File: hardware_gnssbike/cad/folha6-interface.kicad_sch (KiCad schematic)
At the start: 22 parts, among them Q601 DMG1012T-7, Q602 DMG1012T-7, Q603 DMG1012T-7, SW601 XunPu TS-1088R-02026, SW602 XunPu TS-1088R-02026, SW603 XunPu TS-1088R-02026

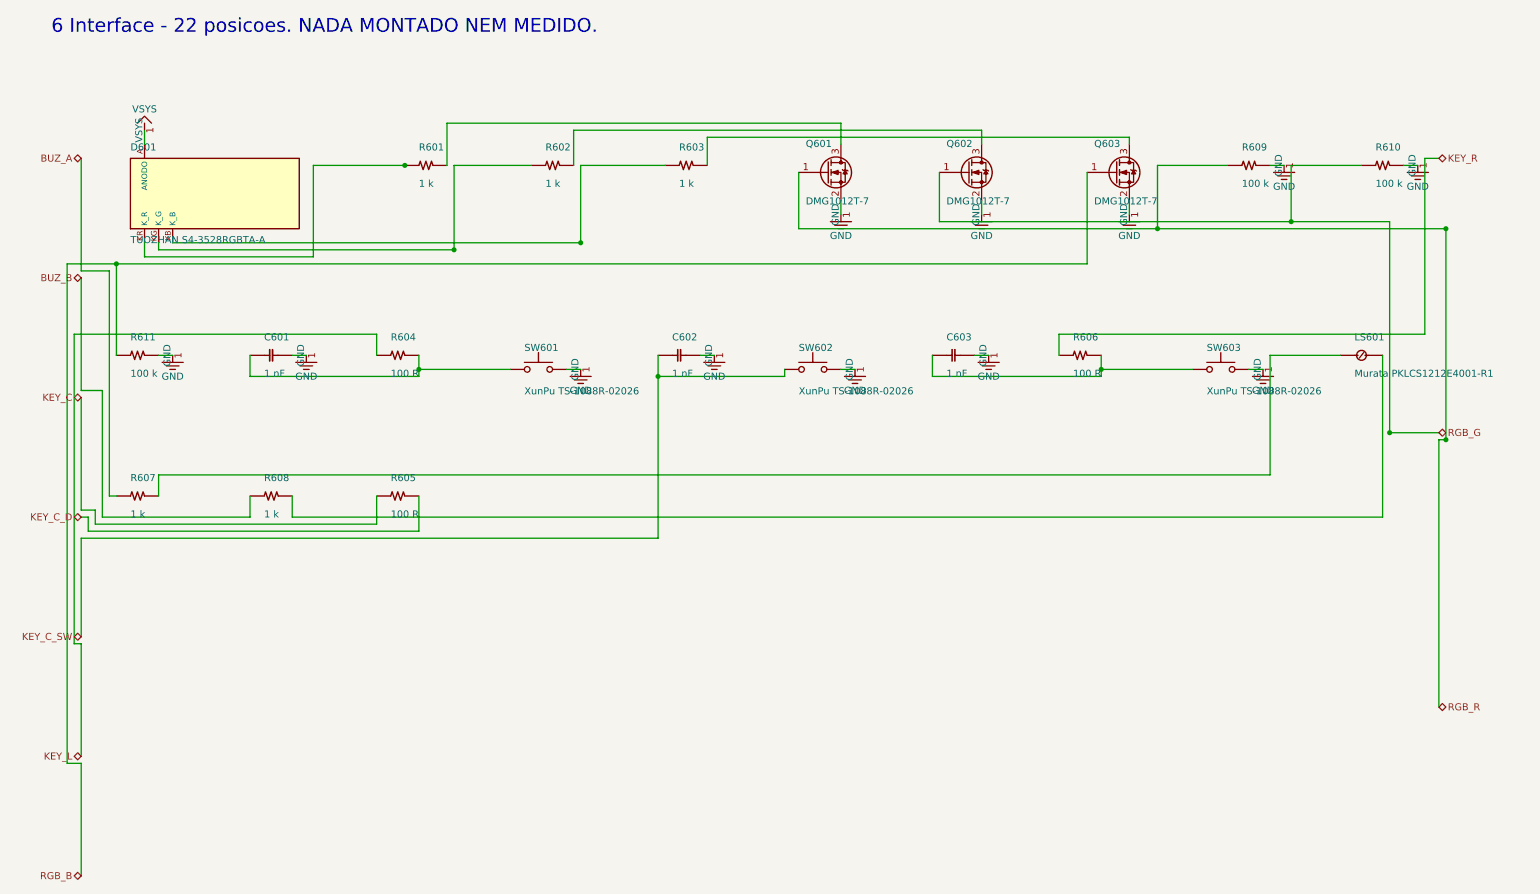
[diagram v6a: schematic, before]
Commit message: feat(hardware): draw the schematic by functional block, the way a person reads it
The owner asked for an industrial-standard schematic: wires and labels,
A4 or A3 pages, the right symbols and values, easy to read, the circuits
subdivided by dashed boxes. Until now each sheet was the netlist drawn as
wires - parts on a grid in connection order and a maze router pulling a
wire from every pin to wherever its other end was, across the page.

blocos.py turns each sheet into a row of functional blocks in the order
the signal flows, each in a dashed rectangle with a title: on the power
sheet, USB-C and protection, the nPM1300, the gauge and the cell, the GNSS
backup, the solar harvester, the thermal cut-off. Membership comes from
the BLOCOS table (the anchors), then make_pcb.DECOPLA and JUNTO (the
board already says whose each capacitor is), then sheets.SEGUE, then the
netlist without rails, nearest anchor by hops. Inside a block the anchor
sits in the middle and each passive beside the pin it serves, on the
side that pin faces, mirrored when the pin that serves the chip is the
far one; parts that touch only rails go to a shelf under the chip. Rails
are power symbols, neighbouring pins of one rail get a wire along their
tips and one symbol; a net that leaves its block is a local label, one
that leaves the sheet a hierarchical label, both on a short stub the
maze router bends when the straight way is taken. Sheet 1 is A3, the
rest A4, measured by the drawing itself. Decoupling capacitors now live
on their chip's sheet whatever their number.

Three KiCad 8 facts were measured with kicad-cli's netlist export on the
way, because the first version assumed each one wrong and check_sch.py
caught it: (mirror x) swaps left for right, not (mirror y); a local label
named after a rail is the net /sheet/RAIL, another net; and a pin in the
middle of a long wire is not on it - "wires connect with other wires or
pins only if their ends coincide exactly" (Eeschema manual). The
conventions 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
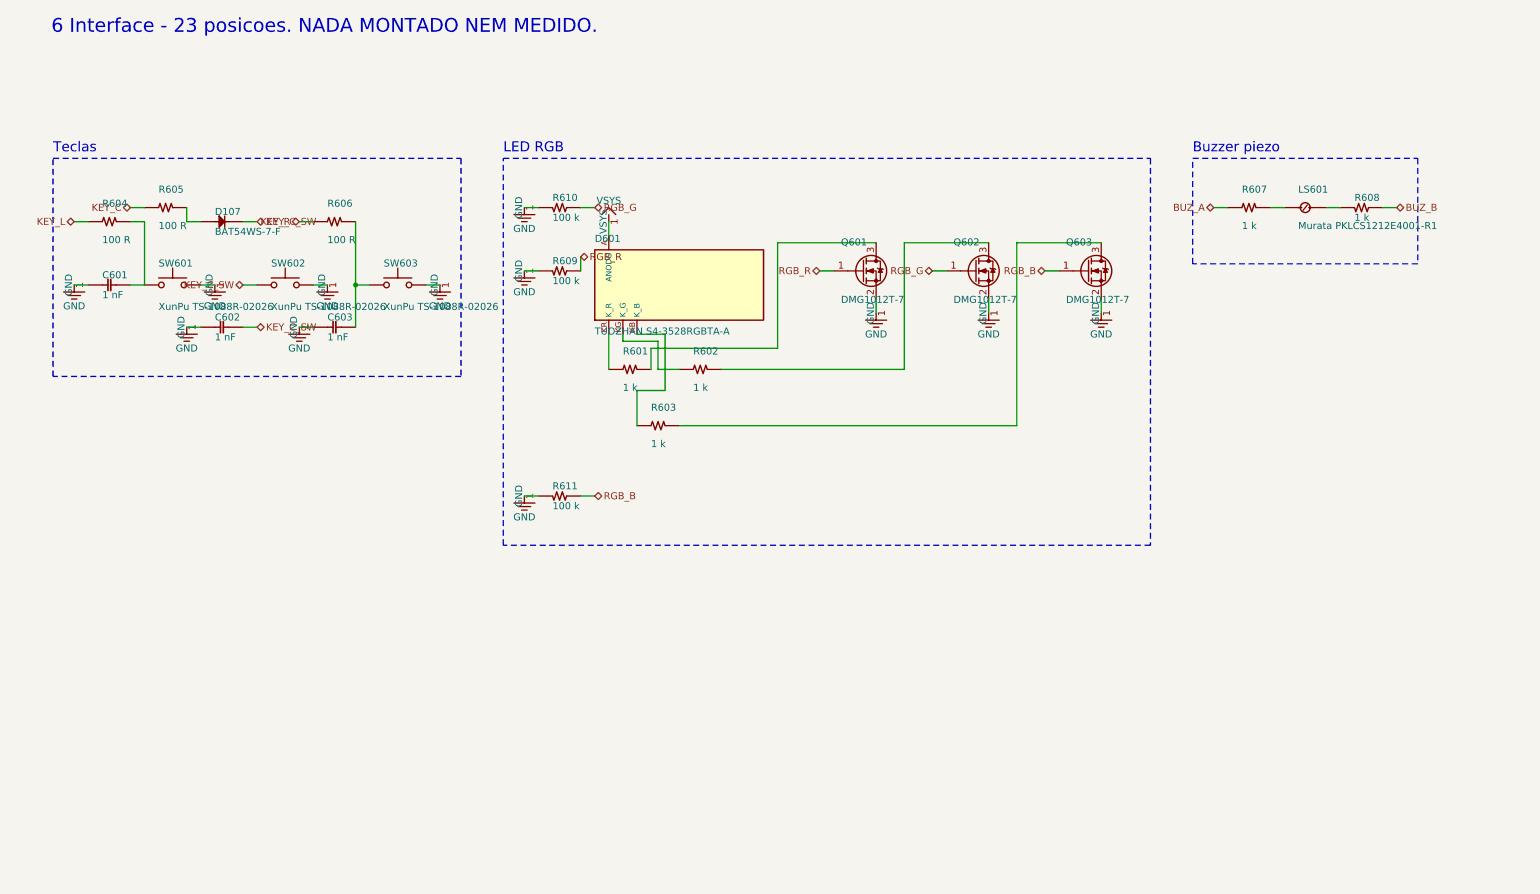
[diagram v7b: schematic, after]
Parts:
- added D107: BAT54WS-7-F, Diode_SMD:D_SOD-323, symbol gnssbike:D107
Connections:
- net KEY_C_SW: now also D107.1 (K)
- net KEY_C_D: no longer names the net of R605.2
- net KEY_C_D: now also D107.2 (A)
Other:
- note added: "6 Interface - 23 posicoes. NADA MONTADO NEM MEDIDO."
- note added: "Buzzer piezo"
- note added: "LED RGB"
- note added: "Teclas"
- note removed: "6 Interface - 22 posicoes. NADA MONTADO NEM MEDIDO."
- moved on the sheet: C601, C602, C603, D601, LS601, Q601, Q602, Q603, R601, R602, R603, R604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

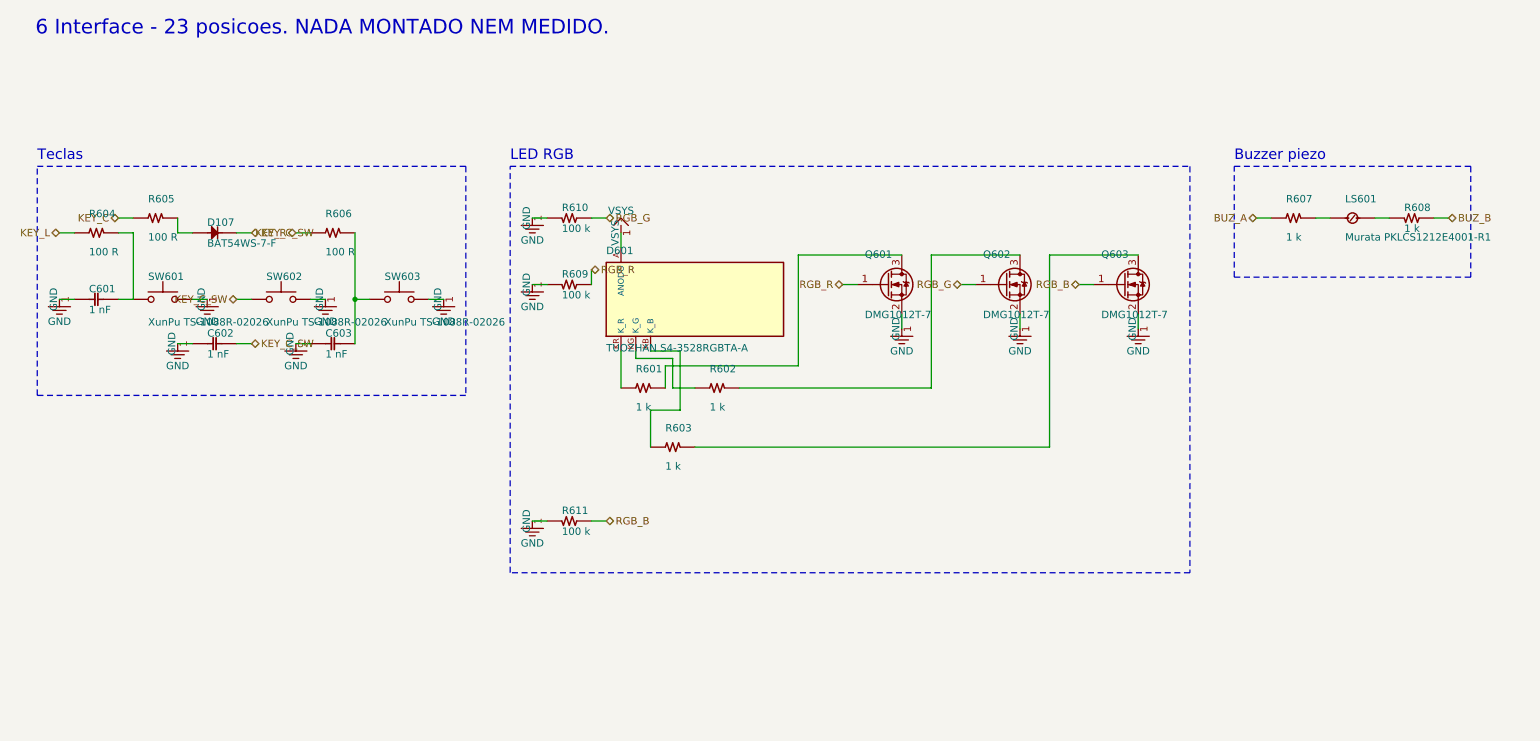
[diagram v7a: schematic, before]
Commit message: feat(hardware): spread the schematic so references, values and labels stay apart
The owner asked for the block-drawn schematic to be readable: designators
and labels were printing over each other. Power symbols now hide the pin
number and name (each printed a "1" and the rail's name twice) and point
away from their pin, lying along the line of a side pin with the name on
that line; the decoupling shelf is a row of stood-up capacitors per rail
with one wire along the tops and one symbol per row, test points standing
too; references and values sit to the right of a standing part and between
the neighbouring lines of a lying one, and block titles, part texts and
symbol names are obstacles for the router and for symbol and label
placement. Pull-ups and pull-downs of a labelled line stand past the label,
and off the corridor when the line goes on to another anchor; the labels'
room is reserved before the members are placed; the FPC connector is
mirrored to face the panel and aligned with it, its board-side wire
continuing from the label point, with the two nets of a pass-through pin
allowed to share cells; the two cells in front of every pin belong to its
net; DISP_VDD is drawn as a rail; blocks are packed by height and sheet 1
fits an A3.

The library symbol now always holds the base drawing and the instance
carries the rotation and mirror. The generator used to write the library
already flipped and the (mirror ...) token as well, applying the transform
twice, and the earlier "measurement" of (mirror x) was inverted by that.
Measured again on minimal files: (mirror y) swaps left for right, an
instance at 90 sends the left pin to the bottom, and KiCad transforms the
field justification along with the instance.

check_sch.py passes: the netlist equals nets.py pin by pin, no new ERC
error, no wire over a component. Eight nets are closed by labels where the
maze found no path inside the block, and the solar harvester and the left
of the gauge remain crowded; SCH_DEBUG=1 exp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
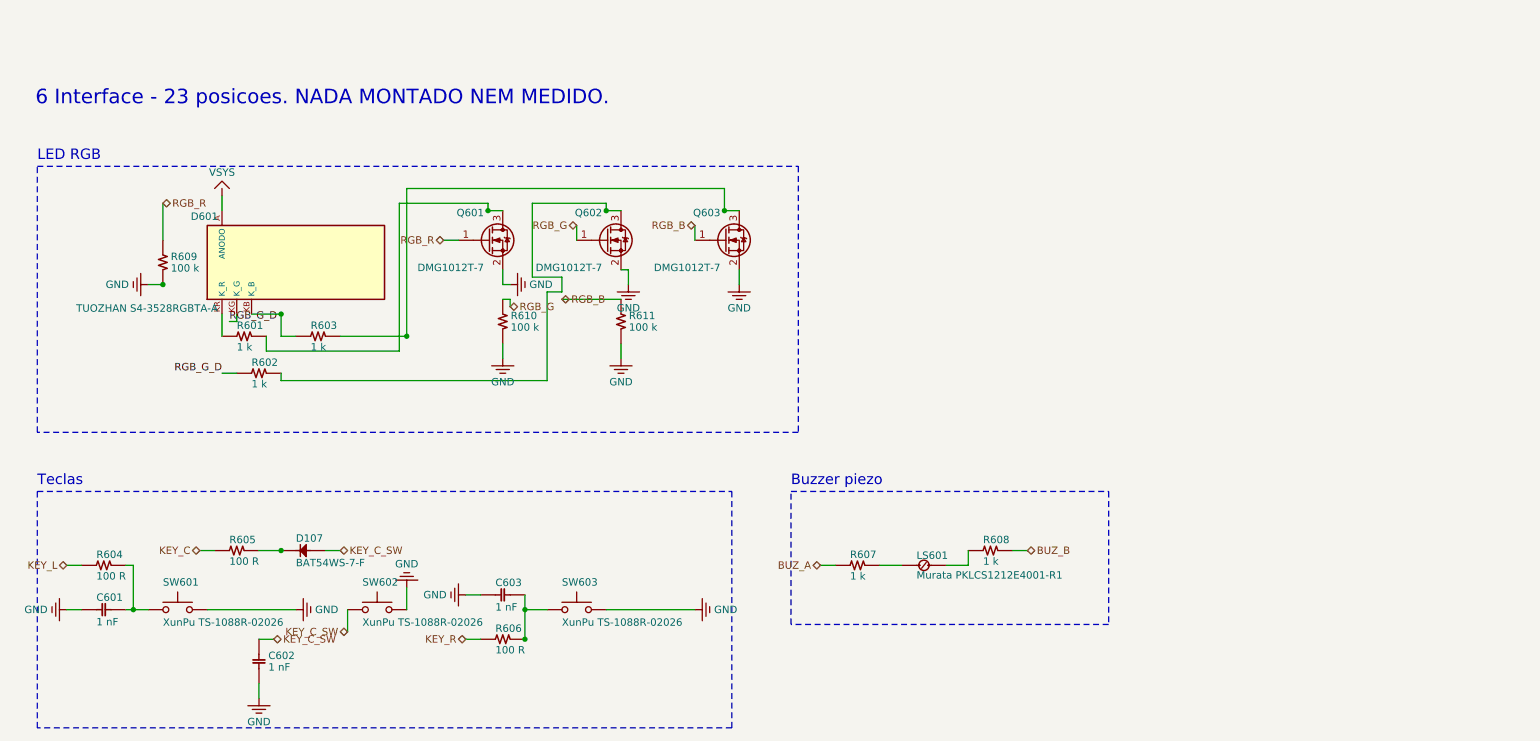
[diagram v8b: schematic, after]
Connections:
- net RGB_G_D: now reaches D601.KG (K_G), R602.1
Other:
- moved on the sheet: C601, C602, C603, D107, D601, LS601, Q601, Q602, Q603, R601, R602, R603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
